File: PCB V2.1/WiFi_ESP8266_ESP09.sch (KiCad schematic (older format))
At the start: 17 parts, among them IC1 ESP_09, P1 CONN_01X04, SW2 B3U-1000P, T1 1909763-1

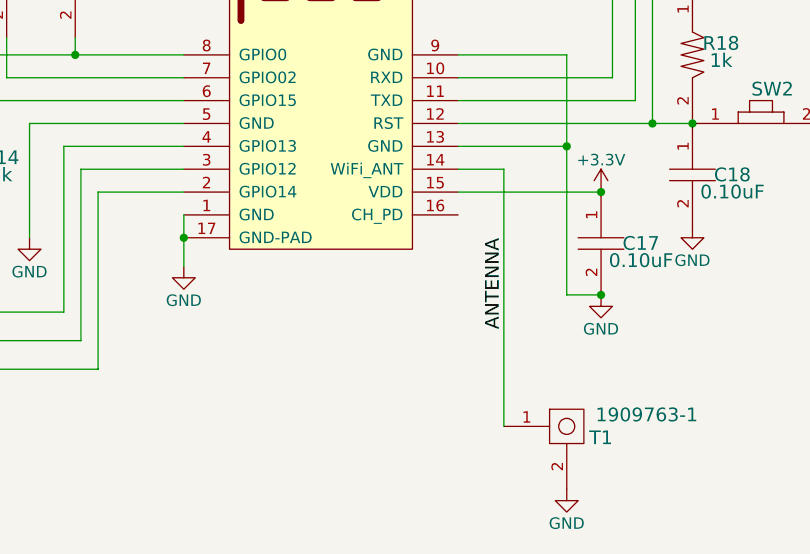
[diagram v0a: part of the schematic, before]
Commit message: 3D and Tweaks
3D files added for components for proper 3D rneder of the board. Board
tweaked, additional ground pours and sticking under neath the ESP-09,
cleaned up routign of JTAG , added labeling of all the pin signals.
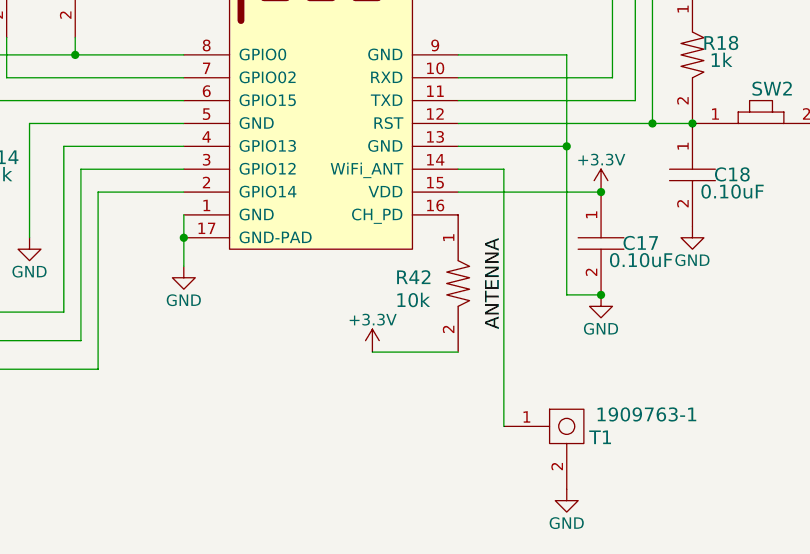
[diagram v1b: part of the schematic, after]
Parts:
- added R42: RC1005F103CS, PCB_Footprints:R0402, symbol RC1005F103CS
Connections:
- net +3V3: now also R42.2
- net at IC1.16 (CH_PD): now also R42.1
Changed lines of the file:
@@
 $EndComp
 $Comp
-L GND #PWR29
+L GND #PWR30
 U 1 1 57D74187
 P 7050 4300
-F 0 "#PWR29" H 7050 4050 50  0001 C CNN
+F 0 "#PWR30" H 7050 4050 50  0001 C CNN
 F 1 "GND" H 7050 4150 50  0000 C CNN
 F 2 "" H 7050 4300 50  0000 C CNN
@@
 $EndComp
 $Comp
-L GND #PWR32
+L GND #PWR33
 U 1 1 57D744DC
 P 8050 3550
-F 0 "#PWR32" H 8050 3300 50  0001 C CNN
+F 0 "#PWR33" H 8050 3300 50  0001 C CNN
 F 1 "GND" H 8050 3400 50  0000 C CNN
 F 2 "" H 8050 3550 50  0000 C CNN
@@
 $EndComp
 $Comp
-L GND #PWR31
+L GND #PWR32
 U 1 1 57D745DC
 P 7450 4000
-F 0 "#PWR31" H 7450 3750 50  0001 C CNN
+F 0 "#PWR32" H 7450 3750 50  0001 C CNN
 F 1 "GND" H 7450 3850 50  0000 C CNN
 F 2 "" H 7450 4000 50  0000 C CNN
@@
 $EndComp
 $Comp
-L GND #PWR27
+L GND #PWR28
 U 1 1 57D74617
 P 6900 5150
-F 0 "#PWR27" H 6900 4900 50  0001 C CNN
+F 0 "#PWR28" H 6900 4900 50  0001 C CNN
 F 1 "GND" H 6900 5000 50  0000 C CNN
 F 2 "" H 6900 5150 50  0000 C CNN
@@
 $EndComp
 $Comp
-L +3.3V #PWR30
+L +3.3V #PWR31
 U 1 1 57D7466A
 P 7450 2950
-F 0 "#PWR30" H 7450 2800 50  0001 C CNN
+F 0 "#PWR31" H 7450 2800 50  0001 C CNN
 F 1 "+3.3V" H 7450 3090 50  0000 C CNN
 F 2 "" H 7450 2950 50  0000 C CNN
@@
 $EndComp
 $Comp
-L GND #PWR33
+L GND #PWR34
 U 1 1 57D7BD68
 P 9100 3075
-F 0 "#PWR33" H 9100 2825 50  0001 C CNN
+F 0 "#PWR34" H 9100 2825 50  0001 C CNN
 F 1 "GND" H 9100 2925 50  0000 C CNN
 F 2 "" H 9100 3075 50  0000 C CNN
@@
 ESP-09 ESP8266 WiFi RF Module
 $Comp
-L +3.3V #PWR28
+L +3.3V #PWR29
 U 1 1 57D94D09
 P 7050 3850
-F 0 "#PWR28" H 7050 3700 50  0001 C CNN
+F 0 "#PWR29" H 7050 3700 50  0001 C CNN
 F 1 "+3.3V" H 7050 3990 50  0000 C CNN
 F 2 "" H 7050 3850 50  0000 C CNN
@@
 Wire Wire Line
 	3975 2300 3600 2300
+$Comp
+L RC1005F103CS R42
+U 1 1 57EC0ECA
+P 6425 4250
+F 0 "R42" V 6400 3975 60  0000 L CNN
+F 1 "RC1005F103CS" V 6425 4338 60  0001 L CNN
+F 2 "PCB_Footprints:R0402" H 6025 4500 60  0001 C CNN
+F 3 "https://media.digikey.com/pdf/Data%20Sheets/Samsung%20PDFs/RC_Series_ds.pdf" H 6125 4700 60  0001 C CNN
+F 4 "0.00173 @ 5000" H 7975 6200 60  0001 C CNN "Cost"
+F 5 "5 Sept 2016" H 6325 4800 60  0001 C CNN "Date Created"
+F 6 "5 Sept 2016" H 6425 4900 60  0001 C CNN "Date Modified"
+F 7 "Adam Vadala-Roth" H 6525 5000 60  0001 C CNN "Designer"
+F 8 "0.4mm" H 6625 5100 60  0001 C CNN "Height"
+F 9 "Yes" H 6725 5200 60  0001 C CNN "RHoS?"
+F 10 "Samsung Electro-Mechanics America, Inc." H 6825 5300 60  0001 C CNN "MFR"
+F 11 "RC1005F103CS" H 6925 5400 60  0001 C CNN "MFR#"
+F 12 "SMT/SMD" H 7025 5500 60  0001 C CNN "Mounting"
+F 13 "2" H 7125 5600 60  0001 C CNN "Pin Count#"
+F 14 "Active" H 7225 5700 60  0001 C CNN "Status"
+F 15 "1%" H 7325 5800 60  0001 C CNN "Tolerance"
+F 16 "passive" H 7425 5900 60  0001 C CNN "Type"
+F 17 "N/A" H 7525 6000 60  0001 C CNN "Voltage"
+F 18 "1/16" H 7625 6100 60  0001 C CNN "Wattage"
+F 19 "10k" V 6500 3975 60  0000 L CNN "Component-Value"
+F 20 "RES SMD 10K OHM 1% 1/16W 0402" H 7825 6300 60  0001 C CNN "Description"
+	1    6425 4250
+	0    1    1    0
+$EndComp
+$Comp
+L +3.3V #PWR27
+U 1 1 57EC13D7
+P 6050 4550
+F 0 "#PWR27" H 6050 4400 50  0001 C CNN
+F 1 "+3.3V" H 6050 4690 50  0000 C CNN
+F 2 "" H 6050 4550 50  0000 C CNN
+F 3 "" H 6050 4550 50  0000 C CNN
+	1    6050 4550
+	1    0    0    -1
+$EndComp
+Wire Wire Line
+	6050 4550 6425 4550
 $EndSCHEMATC

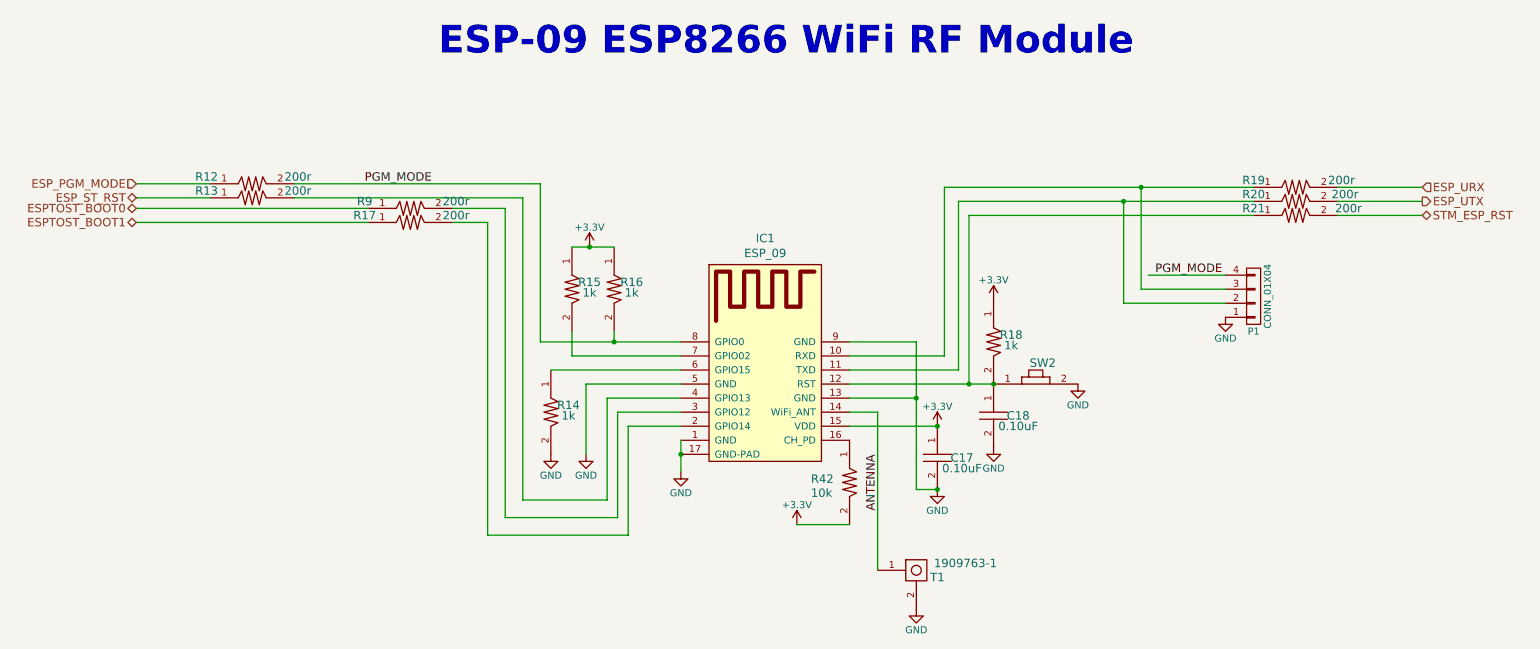
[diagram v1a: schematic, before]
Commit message: Test Points
Test points added as well as some retooling of the PCB overall. More
updates to come before the pending fab
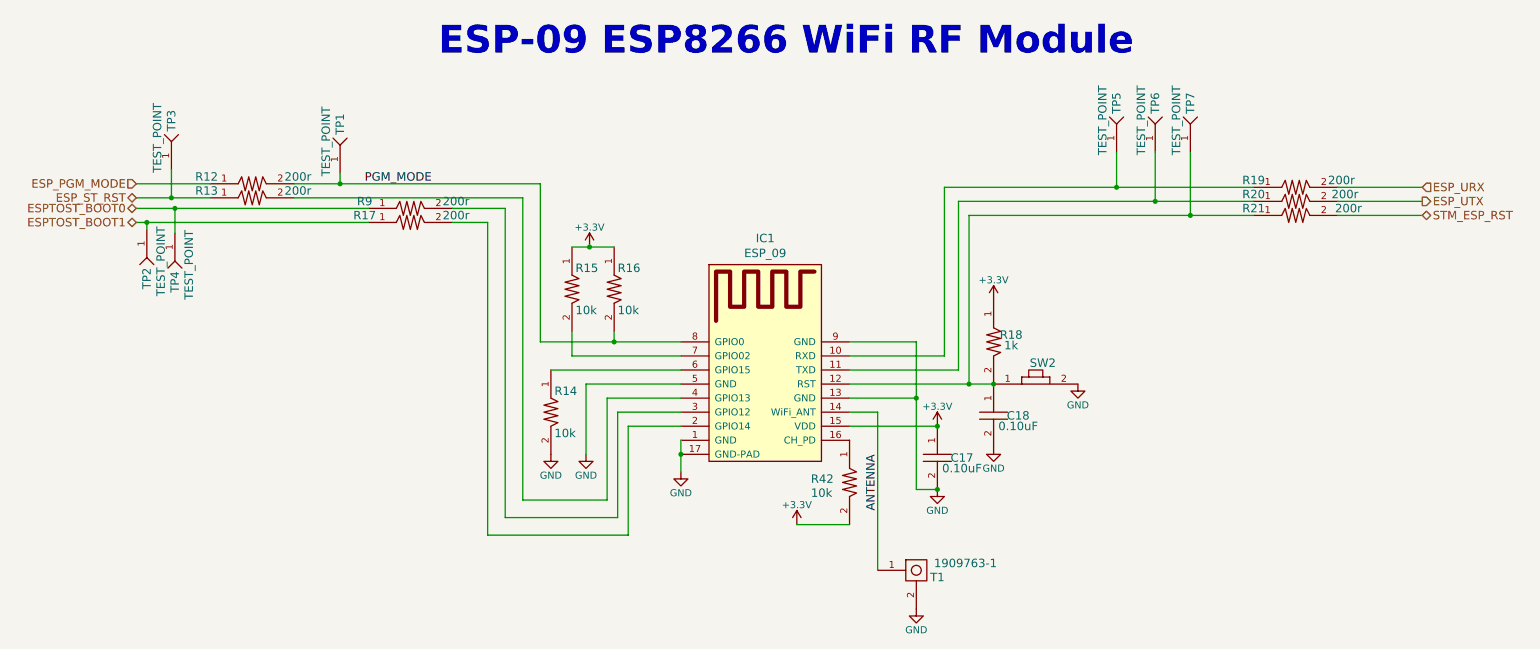
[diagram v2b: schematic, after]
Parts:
- removed P1: CONN_01X04, Pin_Headers:Pin_Header_Straight_1x04, symbol CONN_01X04
- removed R14, R15, R16: RC1005F102CS, PCB_Footprints:R0402, symbol RC1005F102CS
- added R14, R15, R16: RC1005F103CS, PCB_Footprints:R0402, symbol RC1005F103CS
- added TP1, TP2, TP3, TP4, TP5, TP6, TP7: TEST_POINT, PCB_Footprints:TEST_POINT, symbol TEST_POINT
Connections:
- net +3V3: now also R15.1, R16.1
- net ESPTOST_BOOT0: now also TP4.1
- net ESPTOST_BOOT1: now also TP2.1
- net ESP_ST_RST: now also TP3.1
- net GND: now also R14.2
- net PGM_MODE: now also R16.2, TP1.1
- net at C18.1, IC1.12 (RST), R18.2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: now also TP7.1
- net at IC1.10 (RXD), R19.1: now also TP5.1
- net at IC1.11 (TXD), R20.1: now also TP6.1
- net at IC1.7 (GPIO02): now also R15.2
- net at IC1.6 (GPIO15): now also R14.1
